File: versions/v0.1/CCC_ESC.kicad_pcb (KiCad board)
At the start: 4 copper layers, 100 x 65 mm, 155 parts, among them J1 Conn_01x04, J2 Conn_01x04, J3 Conn_01x06, J4 Conn_01x06, U1 NCP5183, U2 NCP5183, U3 NCP5183, U4 NCS20074D, U5 STM32F401CCU6_Balckpill, U6 PQDE6W-Q110, U7 TO220_replacement_module

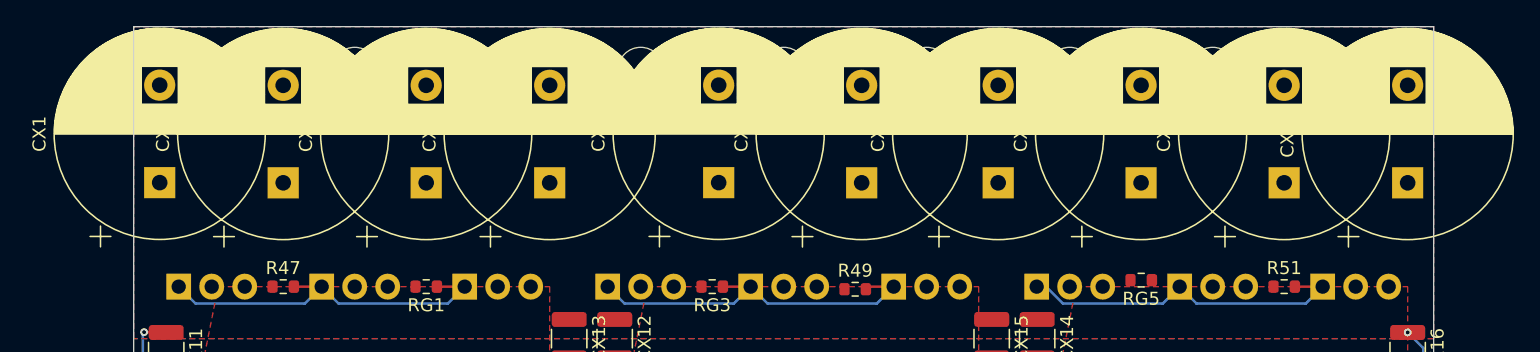
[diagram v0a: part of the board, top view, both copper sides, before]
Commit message: work in progress - added some values and part numbers
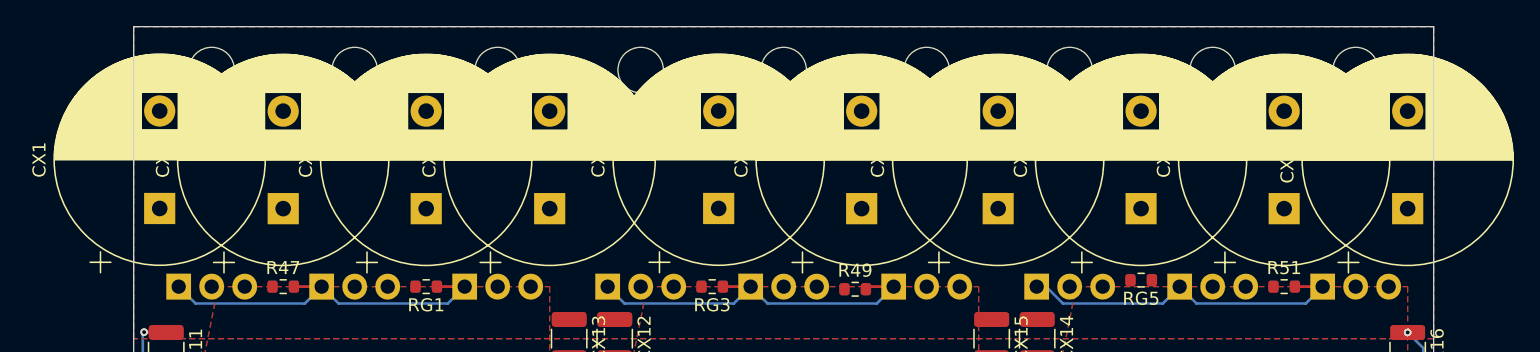
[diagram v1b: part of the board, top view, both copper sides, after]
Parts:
- moved CX1 1.99 mm to (52.0, 64.0)
- moved CX10 1.99 mm to (148.0, 64.0)
- moved CX2 1.99 mm to (61.5, 64.0)
- moved CX3 1.99 mm to (72.5, 64.0)
- moved CX4 1.99 mm to (82.0, 64.0)
- moved CX5 1.99 mm to (95.0, 64.0)
- moved CX6 1.99 mm to (106.0, 64.0)
- moved CX7 1.99 mm to (116.5, 64.0)
- moved CX8 1.99 mm to (138.5, 64.0)
- moved CX9 1.99 mm to (127.5, 64.0)
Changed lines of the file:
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@@
   )
   (footprint "Capacitor_THT:CP_Radial_D16.0mm_P7.50mm" (layer "F.Cu")
-    (at 52 62.000001 90)
+    (at 52 63.987246 90)
     (descr "CP, Radial series, Radial, pin pitch=7.50mm, , diameter=16mm, Electrolytic Capacitor")
     (tags "CP Radial series Radial pin pitch 7.50mm  diameter 16mm Electrolytic Capacitor")
@@
   )
   (footprint "Capacitor_THT:CP_Radial_D16.0mm_P7.50mm" (layer "F.Cu")
-    (at 82 62.012755 90)
+    (at 82 64 90)
     (descr "CP, Radial series, Radial, pin pitch=7.50mm, , diameter=16mm, Electrolytic Capacitor")
     (tags "CP Radial series Radial pin pitch 7.50mm  diameter 16mm Electrolytic Capacitor")
@@
   )
   (footprint "Capacitor_THT:CP_Radial_D16.0mm_P7.50mm" (layer "F.Cu")
-    (at 138.5 62.012755 90)
+    (at 138.5 64 90)
     (descr "CP, Radial series, Radial, pin pitch=7.50mm, , diameter=16mm, Electrolytic Capacitor")
     (tags "CP Radial series Radial pin pitch 7.50mm  diameter 16mm Electrolytic Capacitor")
@@
   )
   (footprint "Capacitor_THT:CP_Radial_D16.0mm_P7.50mm" (layer "F.Cu")
-    (at 148 62.012755 90)
+    (at 148 64 90)
     (descr "CP, Radial series, Radial, pin pitch=7.50mm, , diameter=16mm, Electrolytic Capacitor")
     (tags "CP Radial series Radial pin pitch 7.50mm  diameter 16mm Electrolytic Capacitor")
@@
   )
   (footprint "Capacitor_THT:CP_Radial_D16.0mm_P7.50mm" (layer "F.Cu")
-    (at 127.492754 62.012755 90)
+    (at 127.492754 64 90)
     (descr "CP, Radial series, Radial, pin pitch=7.50mm, , diameter=16mm, Electrolytic Capacitor")
     (tags "CP Radial series Radial pin pitch 7.50mm  diameter 16mm Electrolytic Capacitor")
@@
   )
   (footprint "Capacitor_THT:CP_Radial_D16.0mm_P7.50mm" (layer "F.Cu")
-    (at 116.5 62.012755 90)
+    (at 116.5 64 90)
     (descr "CP, Radial series, Radial, pin pitch=7.50mm, , diameter=16mm, Electrolytic Capacitor")
     (tags "CP Radial series Radial pin pitch 7.50mm  diameter 16mm Electrolytic Capacitor")
@@
   )
   (footprint "Capacitor_THT:CP_Radial_D16.0mm_P7.50mm" (layer "F.Cu")
-    (at 61.5 62.012755 90)
+    (at 61.5 64 90)
     (descr "CP, Radial series, Radial, pin pitch=7.50mm, , diameter=16mm, Electrolytic Capacitor")
     (tags "CP Radial series Radial pin pitch 7.50mm  diameter 16mm Electrolytic Capacitor")
@@
   )
   (footprint "Capacitor_THT:CP_Radial_D16.0mm_P7.50mm" (layer "F.Cu")
-    (at 72.5 62.012755 90)
+    (at 72.5 64 90)
     (descr "CP, Radial series, Radial, pin pitch=7.50mm, , diameter=16mm, Electrolytic Capacitor")
     (tags "CP Radial series Radial pin pitch 7.50mm  diameter 16mm Electrolytic Capacitor")
@@
   )
   (footprint "Capacitor_THT:CP_Radial_D16.0mm_P7.50mm" (layer "F.Cu")
-    (at 95 62.000001 90)
+    (at 95 63.987246 90)
     (descr "CP, Radial series, Radial, pin pitch=7.50mm, , diameter=16mm, Electrolytic Capacitor")
     (tags "CP Radial series Radial pin pitch 7.50mm  diameter 16mm Electrolytic Capacitor")
@@
   )
   (footprint "Capacitor_THT:CP_Radial_D16.0mm_P7.50mm" (layer "F.Cu")
-    (at 106 62.012755 90)
+    (at 106 64 90)
     (descr "CP, Radial series, Radial, pin pitch=7.50mm, , diameter=16mm, Electrolytic Capacitor")
     (tags "CP Radial series Radial pin pitch 7.50mm  diameter 16mm Electrolytic Capacitor")
@@
   (gr_rect (start 76 90) (end 97.5 93) (layer "F.Mask") (width 0.15) (fill solid))
   (gr_rect (start 122.5 72) (end 146 77) (layer "F.Mask") (width 0.15) (fill solid))
-  (gr_rect (start 52 63) (end 147 67) (layer "F.Mask") (width 0.15) (fill solid))
+  (gr_rect (start 52 63.5) (end 147 67.5) (layer "F.Mask") (width 0.15) (fill solid))
   (gr_rect (start 57.5 85) (end 137.5 90) (layer "F.Mask") (width 0.15) (fill solid))
   (gr_rect (start 56.5 72) (end 81.5 77) (layer "F.Mask") (width 0.15) (fill solid))

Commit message: work in progress - added some values and part numbers
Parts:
- removed the C14 at (143.0, 100.5)
- removed the D4 at (109.5, 102.5)
- removed R28: 220k, Resistor_SMD:R_0603_1608Metric
- removed R37, R45, R56: R, Resistor_SMD:R_0805_2012Metric
- removed R38, R46, R57: R, Resistor_SMD:R_0603_1608Metric
- added C15: 1n5, Capacitor_SMD:C_0603_1608Metric, F.Cu at (183.3, 91.5)
- added C29: 47pF, Capacitor_SMD:C_0603_1608Metric, F.Cu at (178.9, 94.0)
- added C30: 47pF, Capacitor_SMD:C_0603_1608Metric, F.Cu at (186.9, 94.0)
- added C31: 47pF, Capacitor_SMD:C_0603_1608Metric, F.Cu at (182.9, 99.0)
- added C4: 1nF, Capacitor_SMD:C_0603_1608Metric, F.Cu at (154.5, 85.1)
- added R10: 100k, Resistor_SMD:R_0805_2012Metric, F.Cu at (166.6, 97.6)
- added R11: 3k3, Resistor_SMD:R_0603_1608Metric, F.Cu at (166.4, 102.8)
- added R2: 2k2, Resistor_SMD:R_0603_1608Metric, F.Cu at (170.8, 96.9)
- added R27: 10k, Resistor_SMD:R_0603_1608Metric, F.Cu at (105.2, 99.2)
- added R3: 1M, Resistor_SMD:R_0805_2012Metric, F.Cu at (152.5, 83.6)
- added R4: 33k, Resistor_SMD:R_0603_1608Metric, F.Cu at (152.5, 86.6)
- added R5: 100k, Resistor_SMD:R_0805_2012Metric, F.Cu at (166.0, 91.4)
- added R6: 3k3, Resistor_SMD:R_0603_1608Metric, F.Cu at (170.4, 102.0)
- added R8: 3k3, Resistor_SMD:R_0603_1608Metric, F.Cu at (175.3, 91.5)
- C14: renamed from C12; value 100n -> 1n5
- C16, C17: value 100n -> 1n5
- CX11, CX12, CX13, CX14, CX15, CX16: value 47uF -> 4.7uF
- R14: value R -> 1M
- R15: value R -> 33k
- R18, R21, R24: value R -> 47k
- R19, R20, R22, R23, R25, R26: value R -> 2k2
- R30, R31, R32: value R -> 22k
- R7: value 2k2 -> 100k; footprint Resistor_SMD:R_0603_1608Metric -> Resistor_SMD:R_0805_2012Metric
- RN1, RN4: value R_Pack04 -> 10k
- RN2, RN3: value R_Pack04 -> 100R
- RN5: value R_Pack04 -> 620R
- SHA1: renamed from R39; value R -> 1mR
- SHA2: renamed from R42; value R -> 1mR
- SHA3: renamed from R53; value R -> 1mR
- SHB1: renamed from R40; value R -> 1mR
- SHB2: renamed from R43; value R -> 1mR
- SHB3: renamed from R54; value R -> 1mR
- SHC1: renamed from R41; value R -> 1mR
- SHC2: renamed from R44; value R -> 1mR
- SHC3: renamed from R55; value R -> 1mR
- moved R24 69.7 mm to (174.9, 94.4), turned to 0 degrees
- moved R32 67.7 mm to (179.3, 91.5), turned to 0 degrees
- moved R26 66.5 mm to (174.5, 102.0), turned to 0 degrees
- moved R21 61.5 mm to (187.3, 91.5)
- moved R25 59.9 mm to (166.4, 100.3), turned to 0 degrees
- moved R20 59.9 mm to (182.9, 96.5), turned to 0 degrees
- moved R31 57.9 mm to (178.9, 101.5), turned to 0 degrees
- moved C9 57.7 mm to (89.5, 114.0), turned to 0 degrees
- moved R23 55.5 mm to (178.9, 96.5), turned to 0 degrees
- moved R19 51.5 mm to (174.9, 99.4)
- moved R22 47.8 mm to (170.8, 94.4)
- moved C17 35.0 mm to (174.9, 96.9), turned to 0 degrees
- moved R7 31.9 mm to (166.6, 94.6), turned to 0 degrees
- moved C16 26.4 mm to (170.8, 99.4), turned to 0 degrees
- moved U7 10.7 mm to (77.0, 109.5), turned to 0 degrees
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- renumbered C13 to C12, C15 to C13, C6 to C5, C5 to C6, C8 to C7, C7 to C8, D5 to D4, D6 to D5, D7 to D6
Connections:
- net Net-(U4-Pad13) renamed VSENSE2
- C18 pad 1: FET_TEMP -> Net-(C18-Pad1)
- JP3 pad 3: Net-(U5-Pad15) -> Net-(C18-Pad1)
- R20 pad 1: A_SHA_V- -> Net-(R20-Pad1)
- R20 pad 2: Net-(U4-Pad2) -> A_SHA_V-
- R23 pad 1: A_SHB_V- -> Net-(R23-Pad1)
- R23 pad 2: Net-(U4-Pad6) -> A_SHB_V-
- R26 pad 1: A_SHC_V- -> Net-(R26-Pad1)
- R26 pad 2: Net-(U4-Pad9) -> A_SHC_V-
- R29 pad 1: Net-(R16-Pad1) -> Net-(R29-Pad1)
- R30 pad 1: Net-(U4-Pad2) -> Net-(R20-Pad1)
- R31 pad 1: Net-(U4-Pad6) -> Net-(R23-Pad1)
- R32 pad 1: Net-(U4-Pad9) -> Net-(R26-Pad1)
- R7 pad 1: Net-(R7-Pad1) -> A_PHB_VSENSE
- R7 pad 2: GND -> PHASE_B
- R9 pad 1: Net-(R9-Pad1) -> GND
- R9 pad 2: GND -> Net-(R9-Pad2)
- RN5 pad 2: A_THROTTLE -> Net-(J1-Pad3)
- RN5 pad 3: Net-(J1-Pad3) -> A_THROTTLE
- RN5 pad 5: Net-(R9-Pad1) -> Net-(R9-Pad2)
- RN5 pad 6: Net-(R9-Pad1) -> Net-(RN5-Pad6)
- RN5 pad 7: Net-(R7-Pad1) -> Net-(R9-Pad2)
- RN5 pad 8: Net-(R7-Pad1) -> Net-(RN5-Pad6)
- U4 pad 12: Net-(R16-Pad1) -> Net-(R29-Pad1)
- U4 pad 2: Net-(U4-Pad2) -> Net-(R20-Pad1)
- U4 pad 6: Net-(U4-Pad6) -> Net-(R23-Pad1)
- U4 pad 9: Net-(U4-Pad9) -> Net-(R26-Pad1)
- U5 pad 15: Net-(U5-Pad15) -> Net-(C18-Pad1)
- U5 pad 18: unconnected-(U5-Pad18) -> V3V3
- U5 pad 28: PA11 DUSB_DM USART6_TX F412_CAN_TX -> unconnected-(U5-Pad28)
- U5 pad 29: PA12 DUSB_DP USART6_RX F412_CAN_TX -> unconnected-(U5-Pad29)
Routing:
- net Net-(R16-Pad1): track 21.0 -> 2.85 mm
- net Net-(R29-Pad1): track 0.00 -> 17.7 mm
- net Net-(U4-Pad9): track 8.42 -> 0.00 mm
- net Net-(R26-Pad1): track 0.00 -> 8.42 mm
- net Net-(U4-Pad6): track 3.92 -> 0.00 mm
- net Net-(R23-Pad1): track 0.00 -> 3.92 mm
- net GND: track 24.7 -> 22.4 mm

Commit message: work in progress - added some values and part numbers
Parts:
- moved R32 67.7 mm to (112.0, 99.0), turned to 90 degrees
- moved R26 66.5 mm to (108.2, 96.0), turned to 90 degrees
- moved R24 65.6 mm to (114.2, 119.4)
- moved R21 61.3 mm to (126.5, 99.5)
- moved R25 60.0 mm to (106.6, 96.0), turned to 90 degrees
- moved R20 59.9 mm to (123.5, 104.0)
- moved R31 57.8 mm to (121.1, 98.7), turned to 90 degrees
- moved R23 55.5 mm to (123.5, 99.5)
- moved R19 51.5 mm to (123.5, 102.5)
- moved R22 46.1 mm to (125.2, 101.0), turned to 180 degrees
- moved C15 41.3 mm to (143.0, 100.5), turned to 90 degrees
- moved R2 35.6 mm to (135.5, 101.3), turned to 90 degrees
- moved C17 35.0 mm to (140.0, 100.5), turned to 90 degrees
- moved R11 32.5 mm to (191.0, 81.6), turned to 90 degrees
- moved R10 31.2 mm to (191.0, 78.1), turned to 90 degrees
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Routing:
- net VSENSE: track 54.3 -> 53.9 mm, vias 4 -> 3

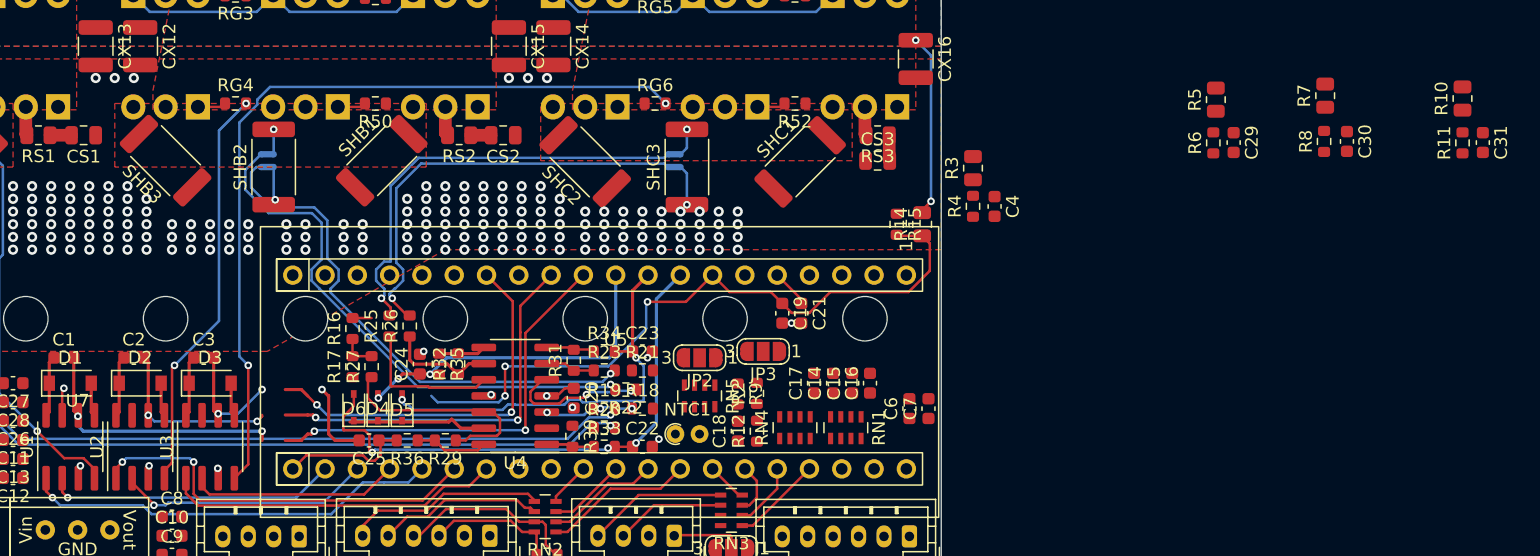
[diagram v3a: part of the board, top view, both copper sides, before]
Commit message: work in progress - added some values and part numbers
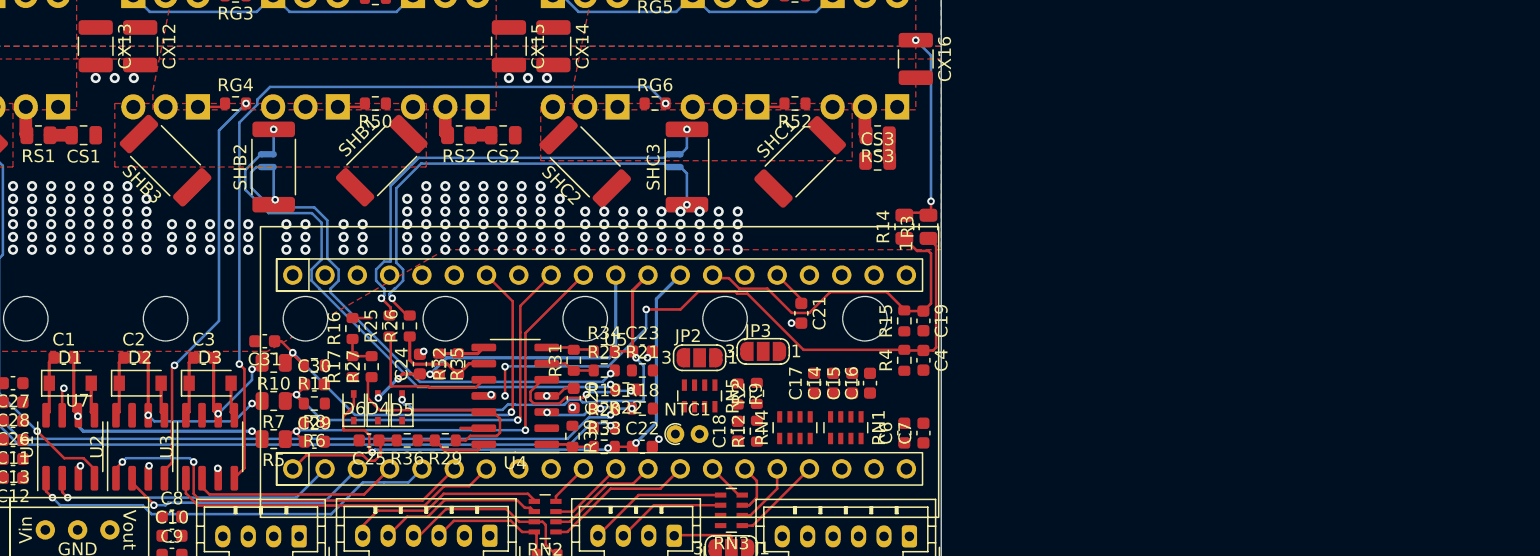
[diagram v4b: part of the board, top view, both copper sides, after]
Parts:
- moved C31 97.1 mm to (96.8, 97.2), turned to 180 degrees
- moved R10 95.8 mm to (97.5, 98.9), turned to 180 degrees
- moved R11 92.0 mm to (100.7, 99.1), turned to 180 degrees
- moved R7 86.1 mm to (97.5, 101.9), turned to 180 degrees
- moved C30 83.4 mm to (100.7, 100.6), turned to 0 degrees
- moved R8 82.0 mm to (100.7, 102.1), turned to 180 degrees
- moved R5 78.8 mm to (97.5, 104.9), turned to 180 degrees
- moved C29 76.0 mm to (100.7, 105.1), turned to 0 degrees
- moved R6 74.0 mm to (100.7, 103.6), turned to 180 degrees
- moved C4 13.3 mm to (148.6, 98.7)
- moved R4 13.3 mm to (147.1, 98.7)
- moved C19 11.1 mm to (148.6, 95.6)
- moved R15 7.62 mm to (147.1, 95.6), turned to 90 degrees
- moved R3 5.79 mm to (149.0, 88.2)
- moved C6 1.97 mm to (147.1, 104.4)
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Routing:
- net VSENSE2: track 10.9 -> 53.0 mm, vias 0 -> 3
- net VSENSE: track 53.9 -> 26.7 mm, vias 3 -> 0
- net GND: track 22.3 -> 15.2 mm, vias 213 -> 212
- net A_PHC_VSENSE: track 30.4 -> 35.2 mm
- net A_PHB_VSENSE: track 30.9 -> 33.8 mm
- net A_PHA_VSENSE: track 33.3 -> 35.3 mm
- net VBAT: track 29.4 -> 31.1 mm
- net PHASE_C: track 12.0 -> 13.4 mm

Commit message: work in progress - pcb work all parts are on the board again
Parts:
- moved C7 46.5 mm to (103.3, 94.0), turned to 180 degrees
- moved R24 24.9 mm to (105.2, 96.2), turned to 90 degrees
- moved D4 3.71 mm to (109.4, 102.6)
- moved D5 3.71 mm to (111.3, 102.6)
- moved D6 3.71 mm to (107.5, 102.6)
- moved R32 0.23 mm to (112.0, 99.2)
- moved C24 0.20 mm to (109.0, 99.2)
- moved R35 0.20 mm to (110.5, 99.2)
- moved R25 0.10 mm to (106.7, 96.0)
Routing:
- net GND: track 15.2 -> 29.0 mm, vias 212 -> 213
- net VSENSE2: track 53.0 -> 63.1 mm, vias 3 -> 4
- net A_SHB_AMP: track 32.5 -> 27.8 mm
- net Net-(R24-Pad1): track 11.3 -> 15.6 mm
- net V3V3: track 3.87 -> 7.75 mm
- net A_SHC_AMP: track 26.9 -> 24.6 mm, vias 3 -> 1
- net A_SHA_AMP: track 42.5 -> 41.2 mm
- net Net-(R29-Pad1): track 17.7 -> 16.6 mm

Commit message: work in progress - pcb work tiny change
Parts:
- moved U7 0.36 mm to (77.4, 109.6)
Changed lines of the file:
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@@
   )
   (footprint "CCC_ESC_Custom_parts:TO220_replacement_module" (layer "F.Cu")
-    (at 77 109.5)
+    (at 77.355 109.555)
     (property "Sheetfile" "CCC_ESC.kicad_sch")
     (property "Sheetname" "")
